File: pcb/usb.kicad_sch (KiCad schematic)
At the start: 36 parts

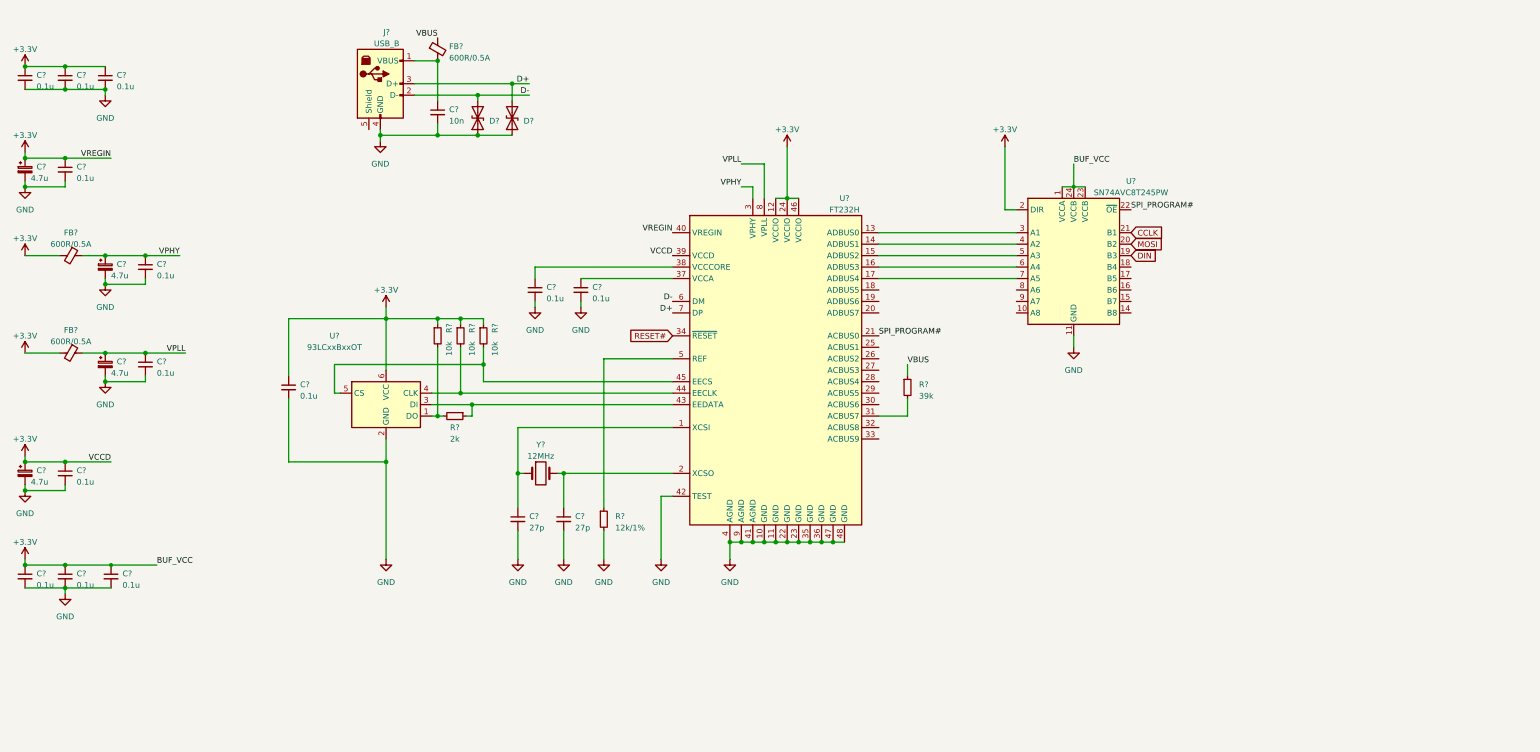
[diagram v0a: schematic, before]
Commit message: add both usb to jtag and usb to spi interface
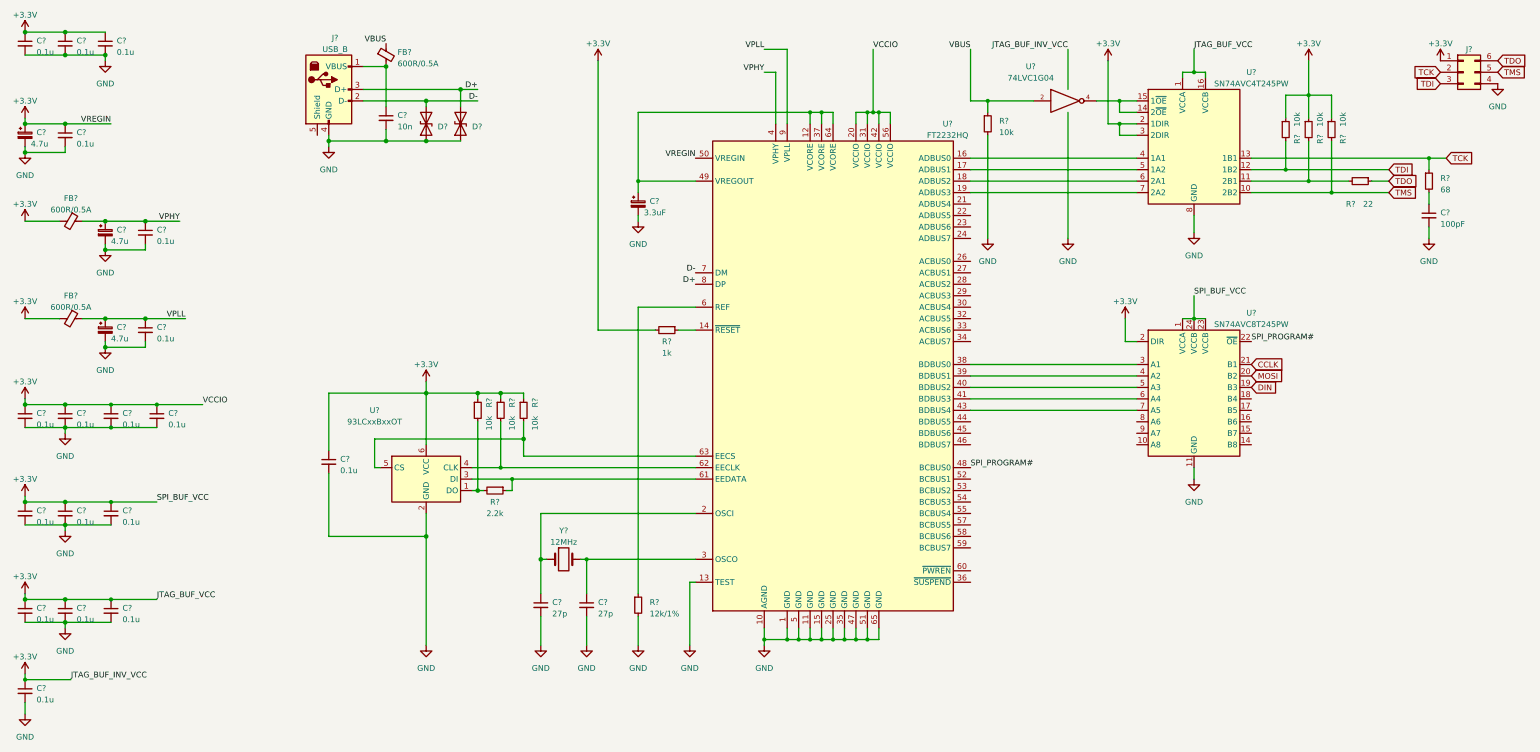
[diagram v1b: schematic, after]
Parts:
- removed C? (x3): 0.1u, symbol Device:C_Small
- removed C?: 4.7u, symbol Device:C_Polarized_Small
- removed R?: 39k, symbol Device:R_Small
- removed U?: FT232H, symbol Interface_USB:FT232H
- added C? (x8): 0.1u, symbol Device:C_Small
- added C?: 3.3uF, symbol Device:C_Polarized_Small
- added C?: 100pF, symbol Device:C_Small
- added J?: Conn_02x03_Counter_Clockwise, symbol Connector_Generic:Conn_02x03_Counter_Clockwise
- added R? (x4): 10k, symbol Device:R_Small
- added R?: 1k, symbol Device:R_Small
- added R?: 22, symbol Device:R_Small
- added R?: 68, symbol Device:R_Small
- added U?: 74LVC1G04, symbol 74xGxx:74LVC1G04
- added U?: SN74AVC4T245PW, Package_SO:TSSOP-16_4.4x5mm_P0.65mm, symbol Logic_LevelTranslator:SN74AVC4T245PW
- added U?: FT2232HQ, Package_DFN_QFN:QFN-64-1EP_9x9mm_P0.5mm_EP4.35x4.35mm, symbol Interface_USB:FT2232HQ
- R?: value 2k -> 2.2k
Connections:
- net +3V3: now also C?.1, C?.1, C?.1, C?.1, C?.1, C?.1, C?.1, C?.1, J?.1 (Pin_1), R?.1, R?.1, R?.1, R?.2, U?.1 (VCCA), U?.16 (VCCB), U?.2 (1DIR), U?.20 (VCCIO), U?.3 (2DIR), U?.31 (VCCIO), U?.42 (VCCIO), U?.5 (VCC), U?.50 (VREGIN), U?.56 (VCCIO)
- net D+: now also U?.8 (DP)
- net D-: now also U?.7 (DM)
- net GND: now also C?.2, C?.2, C?.2, C?.2, C?.2, C?.2, C?.2, C?.2, C?.2, C?.2, J?.4 (Pin_4), R?.2, U?.1 (GND), U?.10 (AGND), U?.11 (GND), U?.13 (TEST), U?.15 (GND), U?.25 (GND), U?.3 (GND), U?.35 (GND), U?.47 (GND), U?.5 (GND), U?.51 (GND), U?.65 (GND), U?.8 (GND), U?.9 (GND)
- net SPI_PROGRAM#: now also U?.48 (BCBUS0)
- net VBUS: now also R?.1, U?.2
- net VPHY: now also U?.4 (VPHY)
- net VPLL: now also U?.9 (VPLL)
- net at R?.1, U?.3 (DI): now also U?.61 (EEDATA)
- net at C?.1, Y?.2: now also U?.3 (OSCO)
- net at R?.1: now also U?.6 (REF)
- net at C?.1, Y?.1: now also U?.2 (OSCI)
- net at U?.3 (A1): now also U?.38 (BDBUS0)
- net at U?.4 (A2): now also U?.39 (BDBUS1)
- net at U?.5 (A3): now also U?.40 (BDBUS2)
- net at U?.6 (A4): now also U?.41 (BDBUS3)
- net at U?.7 (A5): now also U?.43 (BDBUS4)
- net at R?.2, U?.4 (CLK): now also U?.62 (EECLK)
- net at R?.2, U?.5 (CS): now also U?.63 (EECS)
- new net: C?.1, U?.12 (VCORE), U?.37 (VCORE), U?.49 (VREGOUT), U?.64 (VCORE)
- new net: U?.14 (2~OE), U?.15 (1~OE), U?.4
- new net: C?.1, R?.2
- new net: R?.1, U?.14 (~RESET)
- new net: R?.2, R?.2, U?.11 (2B1)
- new net: U?.16 (ADBUS0), U?.4 (1A1)
- new net: U?.17 (ADBUS1), U?.5 (1A2)
- new net: U?.18 (ADBUS2), U?.6 (2A1)
- new net: U?.19 (ADBUS3), U?.7 (2A2)
- new net TCK: J?.2 (Pin_2), R?.1, U?.13 (1B1)
- new net TDI: J?.3 (Pin_3), R?.2, U?.12 (1B2)
- new net TDO: J?.6 (Pin_6), R?.1
- new net TMS: J?.5 (Pin_5), R?.2, U?.10 (2B2)
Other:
- moved on the sheet: C?, D?, FB?, J?, R?, U?, Y?

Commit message: start adding processor fpga
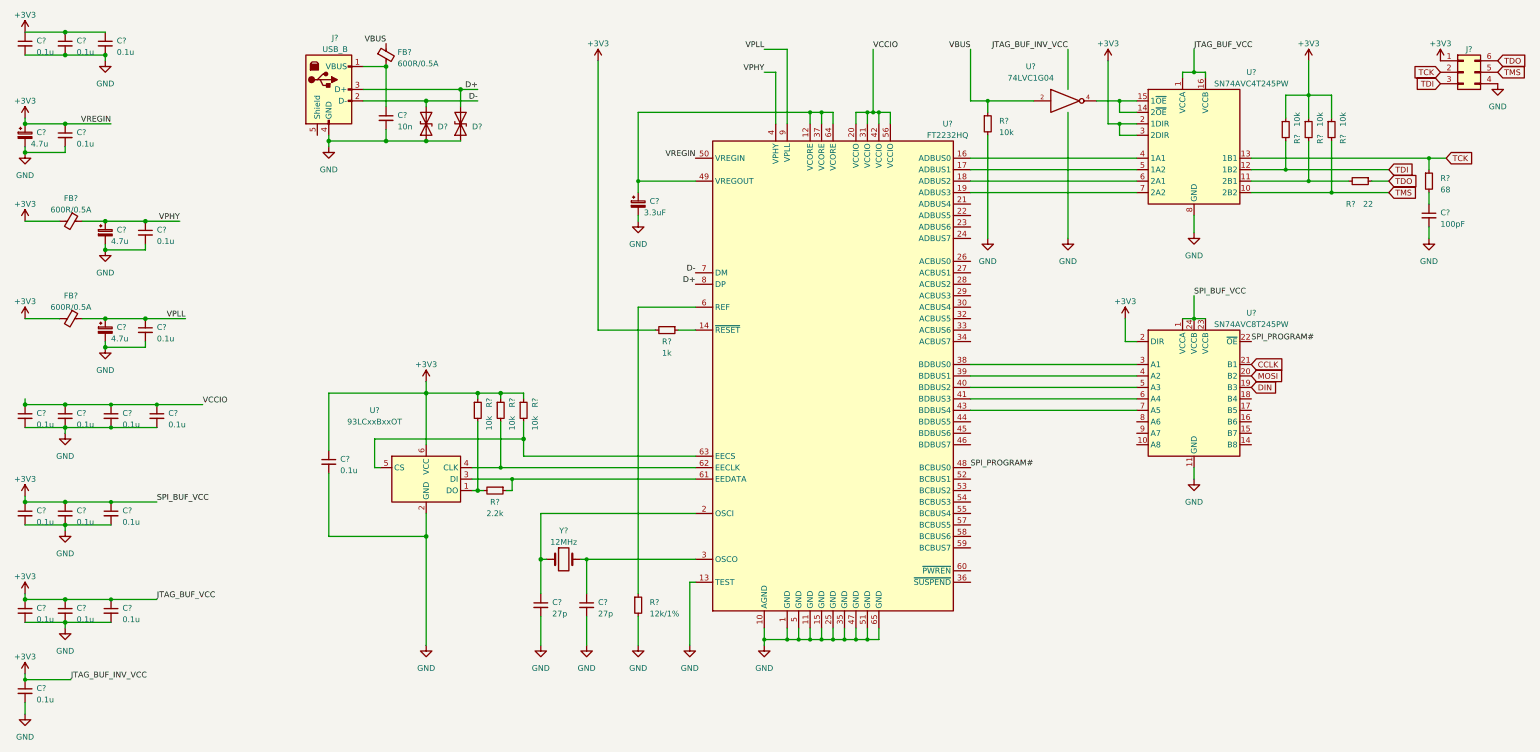
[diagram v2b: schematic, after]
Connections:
- net +3V3: no longer C?.1, C?.1, C?.1, C?.1, U?.20 (VCCIO), U?.31 (VCCIO), U?.42 (VCCIO), U?.56 (VCCIO)
- new net VCCIO: C?.1, C?.1, C?.1, C?.1, U?.20 (VCCIO), U?.31 (VCCIO), U?.42 (VCCIO), U?.56 (VCCIO)
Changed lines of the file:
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@@
     (rev "A")
   )
-  (junction (at 33.02 34.29) (diameter 1.016) (color 0 0 0 0))
   (junction (at 33.02 54.61) (diameter 1.016) (color 0 0 0 0))
   (junction (at 33.02 60.96) (diameter 1.016) (color 0 0 0 0))
@@
     )
   )
-  (symbol (lib_id "power:+3.3V") (at 33.02 34.29 0) (unit 1)
+  (symbol (lib_id "power:+3V3") (at 33.02 34.29 0) (unit 1)
     (in_bom yes) (on_board yes) (fields_autoplaced)
     (property "Reference" "#PWR?" (id 0) (at 33.02 38.1 0)
       (effects (font (size 1.27 1.27)) hide)
     )
-    (property "Value" "+3.3V" (id 1) (at 33.02 30.48 0))
+    (property "Value" "+3V3" (id 1) (at 33.02 30.48 0))
     (property "Footprint" "" (id 2) (at 33.02 34.29 0)
       (effects (font (size 1.27 1.27)) hide)
@@
     (pin "1")
   )
-  (symbol (lib_id "power:+3.3V") (at 33.02 53.34 0) (unit 1)
+  (symbol (lib_id "power:+3V3") (at 33.02 53.34 0) (unit 1)
     (in_bom yes) (on_board yes) (fields_autoplaced)
     (property "Reference" "#PWR?" (id 0) (at 33.02 57.15 0)
       (effects (font (size 1.27 1.27)) hide)
     )
-    (property "Value" "+3.3V" (id 1) (at 33.02 49.53 0))
+    (property "Value" "+3V3" (id 1) (at 33.02 49.53 0))
     (property "Footprint" "" (id 2) (at 33.02 53.34 0)
       (effects (font (size 1.27 1.27)) hide)
@@
     (pin "1")
   )
-  (symbol (lib_id "power:+3.3V") (at 33.02 76.2 0) (unit 1)
+  (symbol (lib_id "power:+3V3") (at 33.02 76.2 0) (unit 1)
     (in_bom yes) (on_board yes) (fields_autoplaced)
     (property "Reference" "#PWR?" (id 0) (at 33.02 80.01 0)
       (effects (font (size 1.27 1.27)) hide)
     )
-    (property "Value" "+3.3V" (id 1) (at 33.02 72.39 0))
+    (property "Value" "+3V3" (id 1) (at 33.02 72.39 0))
     (property "Footprint" "" (id 2) (at 33.02 76.2 0)
       (effects (font (size 1.27 1.27)) hide)
@@
     (pin "1")
   )
-  (symbol (lib_id "power:+3.3V") (at 33.02 97.79 0) (unit 1)
+  (symbol (lib_id "power:+3V3") (at 33.02 97.79 0) (unit 1)
     (in_bom yes) (on_board yes) (fields_autoplaced)
     (property "Reference" "#PWR?" (id 0) (at 33.02 101.6 0)
       (effects (font (size 1.27 1.27)) hide)
     )
-    (property "Value" "+3.3V" (id 1) (at 33.02 93.98 0))
+    (property "Value" "+3V3" (id 1) (at 33.02 93.98 0))
     (property "Footprint" "" (id 2) (at 33.02 97.79 0)
       (effects (font (size 1.27 1.27)) hide)
@@
     (pin "1")
   )
-  (symbol (lib_id "power:+3.3V") (at 33.02 115.57 0) (unit 1)
-    (in_bom yes) (on_board yes) (fields_autoplaced)
-    (property "Reference" "#PWR?" (id 0) (at 33.02 119.38 0)
-      (effects (font (size 1.27 1.27)) hide)
-    )
-    (property "Value" "+3.3V" (id 1) (at 33.02 111.76 0))
-    (property "Footprint" "" (id 2) (at 33.02 115.57 0)
-      (effects (font (size 1.27 1.27)) hide)
-    )
-    (property "Datasheet" "" (id 3) (at 33.02 115.57 0)
-      (effects (font (size 1.27 1.27)) hide)
-    )
-    (pin "1")
-  )
-  (symbol (lib_id "power:+3.3V") (at 33.02 137.16 0) (unit 1)
+  (symbol (lib_id "power:+3V3") (at 33.02 137.16 0) (unit 1)
     (in_bom yes) (on_board yes) (fields_autoplaced)
     (property "Reference" "#PWR?" (id 0) (at 33.02 140.97 0)
       (effects (font (size 1.27 1.27)) hide)
     )
-    (property "Value" "+3.3V" (id 1) (at 33.02 133.35 0))
+    (property "Value" "+3V3" (id 1) (at 33.02 133.35 0))
     (property "Footprint" "" (id 2) (at 33.02 137.16 0)
       (effects (font (size 1.27 1.27)) hide)
@@
     (pin "1")
   )
-  (symbol (lib_id "power:+3.3V") (at 33.02 158.75 0) (unit 1)
+  (symbol (lib_id "power:+3V3") (at 33.02 158.75 0) (unit 1)
     (in_bom yes) (on_board yes) (fields_autoplaced)
     (property "Reference" "#PWR?" (id 0) (at 33.02 162.56 0)
       (effects (font (size 1.27 1.27)) hide)
     )
-    (property "Value" "+3.3V" (id 1) (at 33.02 154.94 0))
+    (property "Value" "+3V3" (id 1) (at 33.02 154.94 0))
     (property "Footprint" "" (id 2) (at 33.02 158.75 0)
       (effects (font (size 1.27 1.27)) hide)
@@
     (pin "1")
   )
-  (symbol (lib_id "power:+3.3V") (at 33.02 176.53 0) (unit 1)
+  (symbol (lib_id "power:+3V3") (at 33.02 176.53 0) (unit 1)
     (in_bom yes) (on_board yes) (fields_autoplaced)
     (property "Reference" "#PWR?" (id 0) (at 33.02 180.34 0)
       (effects (font (size 1.27 1.27)) hide)
     )
-    (property "Value" "+3.3V" (id 1) (at 33.02 172.72 0))
+    (property "Value" "+3V3" (id 1) (at 33.02 172.72 0))
     (property "Footprint" "" (id 2) (at 33.02 176.53 0)
       (effects (font (size 1.27 1.27)) hide)
@@
     (pin "1")
   )
-  (symbol (lib_id "power:+3.3V") (at 121.92 111.76 0) (unit 1)
+  (symbol (lib_id "power:+3V3") (at 121.92 111.76 0) (unit 1)
     (in_bom yes) (on_board yes) (fields_autoplaced)
     (property "Reference" "#PWR?" (id 0) (at 121.92 115.57 0)
       (effects (font (size 1.27 1.27)) hide)
     )
-    (property "Value" "+3.3V" (id 1) (at 121.92 107.95 0))
+    (property "Value" "+3V3" (id 1) (at 121.92 107.95 0))
     (property "Footprint" "" (id 2) (at 121.92 111.76 0)
       (effects (font (size 1.27 1.27)) hide)
@@
     (pin "1")
   )
-  (symbol (lib_id "power:+3.3V") (at 160.02 40.64 0) (unit 1)
+  (symbol (lib_id "power:+3V3") (at 160.02 40.64 0) (unit 1)
     (in_bom yes) (on_board yes) (fields_autoplaced)
     (property "Reference" "#PWR?" (id 0) (at 160.02 44.45 0)
       (effects (font (size 1.27 1.27)) hide)
     )
-    (property "Value" "+3.3V" (id 1) (at 160.02 36.83 0))
+    (property "Value" "+3V3" (id 1) (at 160.02 36.83 0))
     (property "Footprint" "" (id 2) (at 160.02 40.64 0)
       (effects (font (size 1.27 1.27)) hide)
@@
     (pin "1")
   )
-  (symbol (lib_id "power:+3.3V") (at 273.05 40.64 0) (unit 1)
+  (symbol (lib_id "power:+3V3") (at 273.05 40.64 0) (unit 1)
     (in_bom yes) (on_board yes) (fields_autoplaced)
     (property "Reference" "#PWR?" (id 0) (at 273.05 44.45 0)
       (effects (font (size 1.27 1.27)) hide)
     )
-    (property "Value" "+3.3V" (id 1) (at 273.05 36.83 0))
+    (property "Value" "+3V3" (id 1) (at 273.05 36.83 0))
     (property "Footprint" "" (id 2) (at 273.05 40.64 0)
       (effects (font (size 1.27 1.27)) hide)
@@
     (pin "1")
   )
-  (symbol (lib_id "power:+3.3V") (at 276.86 97.79 0) (unit 1)
+  (symbol (lib_id "power:+3V3") (at 276.86 97.79 0) (unit 1)
     (in_bom yes) (on_board yes) (fields_autoplaced)
     (property "Reference" "#PWR?" (id 0) (at 276.86 101.6 0)
       (effects (font (size 1.27 1.27)) hide)
     )
-    (property "Value" "+3.3V" (id 1) (at 276.86 93.98 0))
+    (property "Value" "+3V3" (id 1) (at 276.86 93.98 0))
     (property "Footprint" "" (id 2) (at 276.86 97.79 0)
       (effects (font (size 1.27 1.27)) hide)
@@
     (pin "1")
   )
-  (symbol (lib_id "power:+3.3V") (at 317.5 40.64 0) (unit 1)
+  (symbol (lib_id "power:+3V3") (at 317.5 40.64 0) (unit 1)
     (in_bom yes) (on_board yes) (fields_autoplaced)
     (property "Reference" "#PWR?" (id 0) (at 317.5 44.45 0)
       (effects (font (size 1.27 1.27)) hide)
     )
-    (property "Value" "+3.3V" (id 1) (at 317.5 36.83 0))
+    (property "Value" "+3V3" (id 1) (at 317.5 36.83 0))
     (property "Footprint" "" (id 2) (at 317.5 40.64 0)
       (effects (font (size 1.27 1.27)) hide)
@@
     (pin "1")
   )
-  (symbol (lib_id "power:+3.3V") (at 346.71 40.64 0) (unit 1)
+  (symbol (lib_id "power:+3V3") (at 346.71 40.64 0) (unit 1)
     (in_bom yes) (on_board yes) (fields_autoplaced)
     (property "Reference" "#PWR?" (id 0) (at 346.71 44.45 0)
       (effects (font (size 1.27 1.27)) hide)
     )
-    (property "Value" "+3.3V" (id 1) (at 346.71 36.83 0))
+    (property "Value" "+3V3" (id 1) (at 346.71 36.83 0))
     (property "Footprint" "" (id 2) (at 346.71 40.64 0)
       (effects (font (size 1.27 1.27)) hide)

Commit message: add flash memory
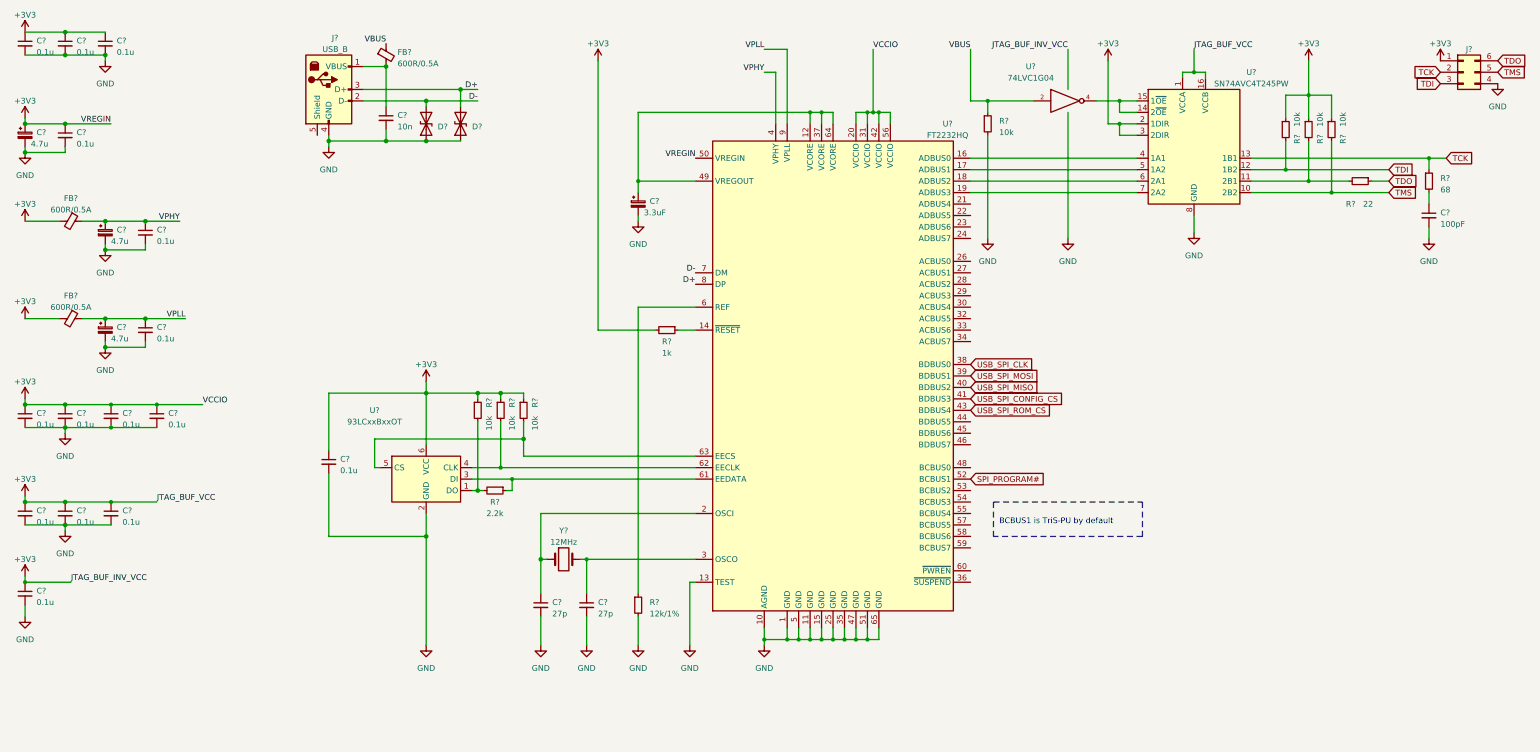
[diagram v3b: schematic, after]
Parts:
- removed C? (x3): 0.1u, symbol Device:C_Small
- removed U?: SN74AVC8T245PW, Package_SO:TSSOP-24_4.4x7.8mm_P0.65mm, symbol Logic_LevelTranslator:SN74AVC8T245PW
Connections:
- net VCCIO is gone; now on net +3V3: C?.1, C?.1, C?.1, C?.1, U?.20 (VCCIO), U?.31 (VCCIO), U?.42 (VCCIO), U?.56 (VCCIO)
- net SPI_PROGRAM#: now also U?.52 (BCBUS1); no longer U?.48 (BCBUS0)
- net USB_SPI_CLK: now reaches U?.38 (BDBUS0)
- net USB_SPI_MOSI: now reaches U?.39 (BDBUS1)
- net USB_SPI_MISO: now reaches U?.40 (BDBUS2)
- net USB_SPI_CONFIG_CS: now reaches U?.41 (BDBUS3)
- net USB_SPI_ROM_CS: now reaches U?.43 (BDBUS4)
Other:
- note added: "BCBUS1 is TriS-PU by default"
- moved on the sheet: C?

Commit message: start associating footprints
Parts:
- C28, C29, C30, C31, C33, C35, C37, C39, C40, C41, C42, C43, C44, C45, C46, C47, C48, C49, C50: renamed from C?; footprint (none) -> Capacitor_SMD:C_0402_1005Metric
- C32: renamed from C?; footprint (none) -> Capacitor_SMD:CP_Elec_4x4.5; Ref (none) -> EDK475M025A9BAA
- C34: renamed from C?; footprint (none) -> Capacitor_SMD:CP_Elec_4x4.5; Ref (none) -> 865090640007
- C36, C38: renamed from C?; footprint (none) -> Capacitor_SMD:CP_Elec_4x4.5
- D1: renamed from D?; footprint (none) -> Package_SO:DO-214AC; Ref (none) -> P6SMB9.1CA-Q
- D2: renamed from D?; footprint (none) -> Package_SO:DO-214AC
- FB1: renamed from FB?; footprint (none) -> Inductor_SMD:L_0603_1608Metric; Ref (none) -> 742863160
- FB2, FB3: renamed from FB?; footprint (none) -> Inductor_SMD:L_0603_1608Metric
- J2: renamed from J?; Ref (none) -> SS-52300-001
- gave numbers to parts that had none: 18
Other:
- moved on the sheet: C33
